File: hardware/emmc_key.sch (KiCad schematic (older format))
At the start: 7 parts, among them U1 EMMC Module

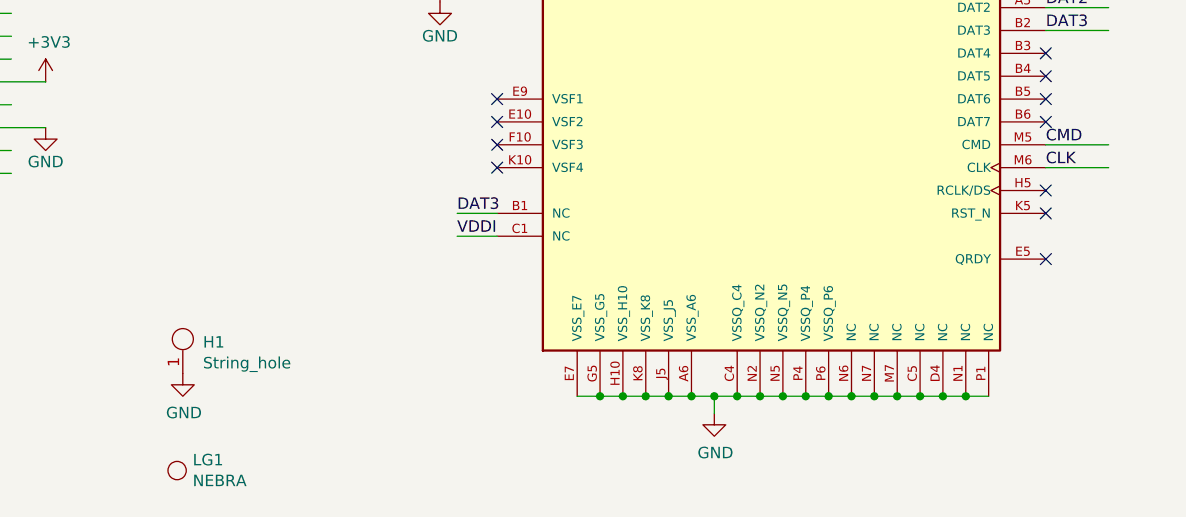
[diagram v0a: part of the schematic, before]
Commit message: RST_N connected to 3V3. Fabrication outputs regenerated.
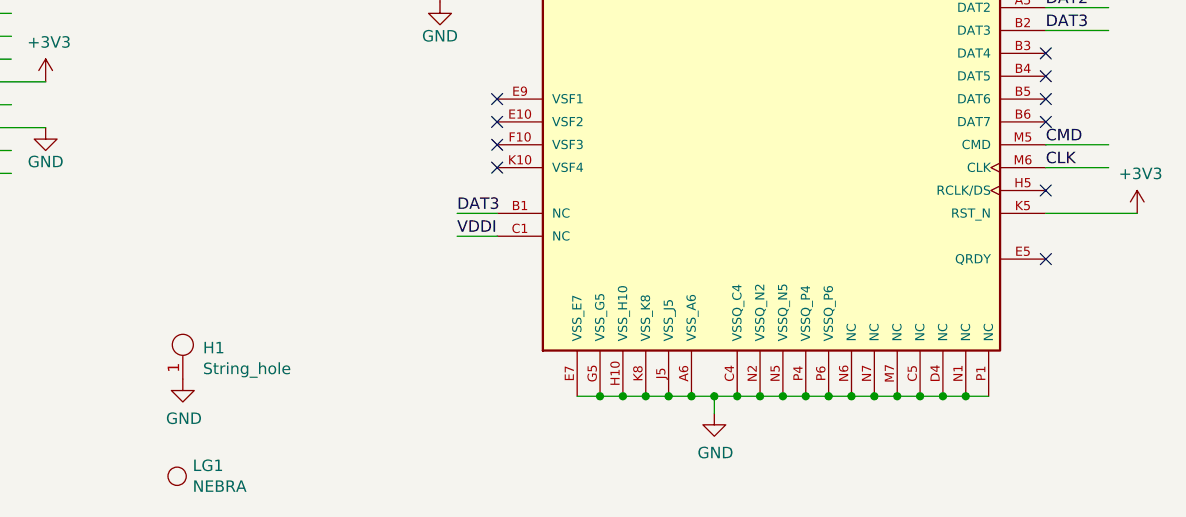
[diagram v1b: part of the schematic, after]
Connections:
- wire segments 54 -> 55
- no-connect marks 11 -> 10
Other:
- moved on the sheet: H1, LG1
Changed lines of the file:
@@
 NoConn ~ 7875 3750
 NoConn ~ 7875 4050
-NoConn ~ 7875 4150
 NoConn ~ 7875 4350
 NoConn ~ 5475 3850
@@
 L emms_key:String_hole H1
 U 1 1 607B301D
-P 4100 4700
-F 0 "H1" V 4114 4788 50  0000 L CNN
-F 1 "String_hole" V 4205 4788 50  0000 L CNN
-F 2 "MountingHole:MountingHole_2.2mm_M2" H 4100 4700 50  0001 C CNN
-F 3 "" H 4100 4700 50  0001 C CNN
-	1    4100 4700
+P 4100 4725
+F 0 "H1" V 4114 4813 50  0000 L CNN
+F 1 "String_hole" V 4205 4813 50  0000 L CNN
+F 2 "MountingHole:MountingHole_2.2mm_M2" H 4100 4725 50  0001 C CNN
+F 3 "" H 4100 4725 50  0001 C CNN
+	1    4100 4725
 	0    1    1    0
 $EndComp
@@
 L power:GND #PWR0108
 U 1 1 607B424A
-P 4100 4850
-F 0 "#PWR0108" H 4100 4600 50  0001 C CNN
-F 1 "GND" H 4105 4677 50  0000 C CNN
-F 2 "" H 4100 4850 50  0001 C CNN
-F 3 "" H 4100 4850 50  0001 C CNN
-	1    4100 4850
+P 4100 4875
+F 0 "#PWR0108" H 4100 4625 50  0001 C CNN
+F 1 "GND" H 4105 4702 50  0000 C CNN
+F 2 "" H 4100 4875 50  0001 C CNN
+F 3 "" H 4100 4875 50  0001 C CNN
+	1    4100 4875
 	1    0    0    -1
 $EndComp
@@
 L emms_key:Logo LG1
 U 1 1 607BEA9F
-P 4075 5275
-F 0 "LG1" H 4143 5321 50  0000 L CNN
-F 1 "NEBRA" H 4143 5230 50  0000 L CNN
-F 2 "emmc_key:NEBRA_LOGO" H 3895 5280 50  0001 C CNN
-F 3 "" H 3895 5280 50  0001 C CNN
-	1    4075 5275
+P 4075 5300
+F 0 "LG1" H 4143 5346 50  0000 L CNN
+F 1 "NEBRA" H 4143 5255 50  0000 L CNN
+F 2 "emmc_key:NEBRA_LOGO" H 3895 5305 50  0001 C CNN
+F 3 "" H 3895 5305 50  0001 C CNN
+	1    4075 5300
 	1    0    0    -1
 $EndComp
@@
 Wire Wire Line
 	7525 4950 7625 4950
+$Comp
+L power:+3V3 #PWR?
+U 1 1 60C0D36F
+P 8275 4150
+F 0 "#PWR?" H 8275 4000 50  0001 C CNN
+F 1 "+3V3" H 8290 4323 50  0000 C CNN
+F 2 "" H 8275 4150 50  0001 C CNN
+F 3 "" H 8275 4150 50  0001 C CNN
+	1    8275 4150
+	1    0    0    -1
+$EndComp
+Wire Wire Line
+	7875 4150 8275 4150
 $EndSCHEMATC

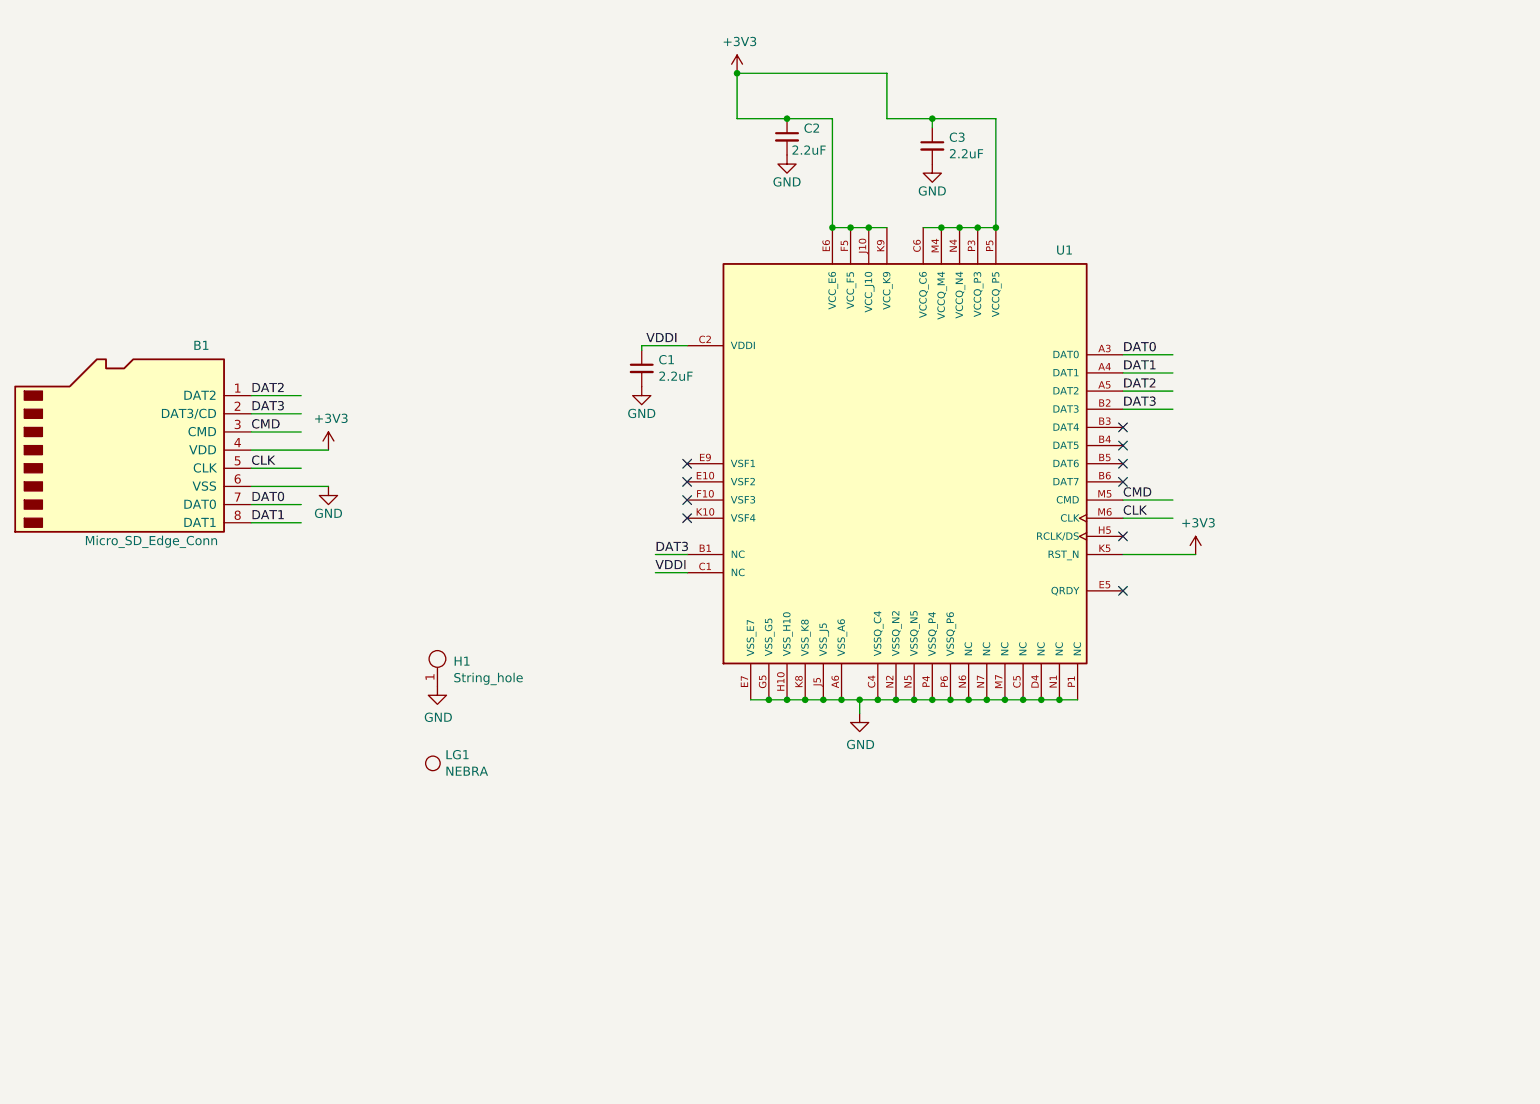
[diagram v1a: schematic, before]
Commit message: New variant with voltage translator and 1V8 LDO for eMMC modules where VCCQ is 1V8.
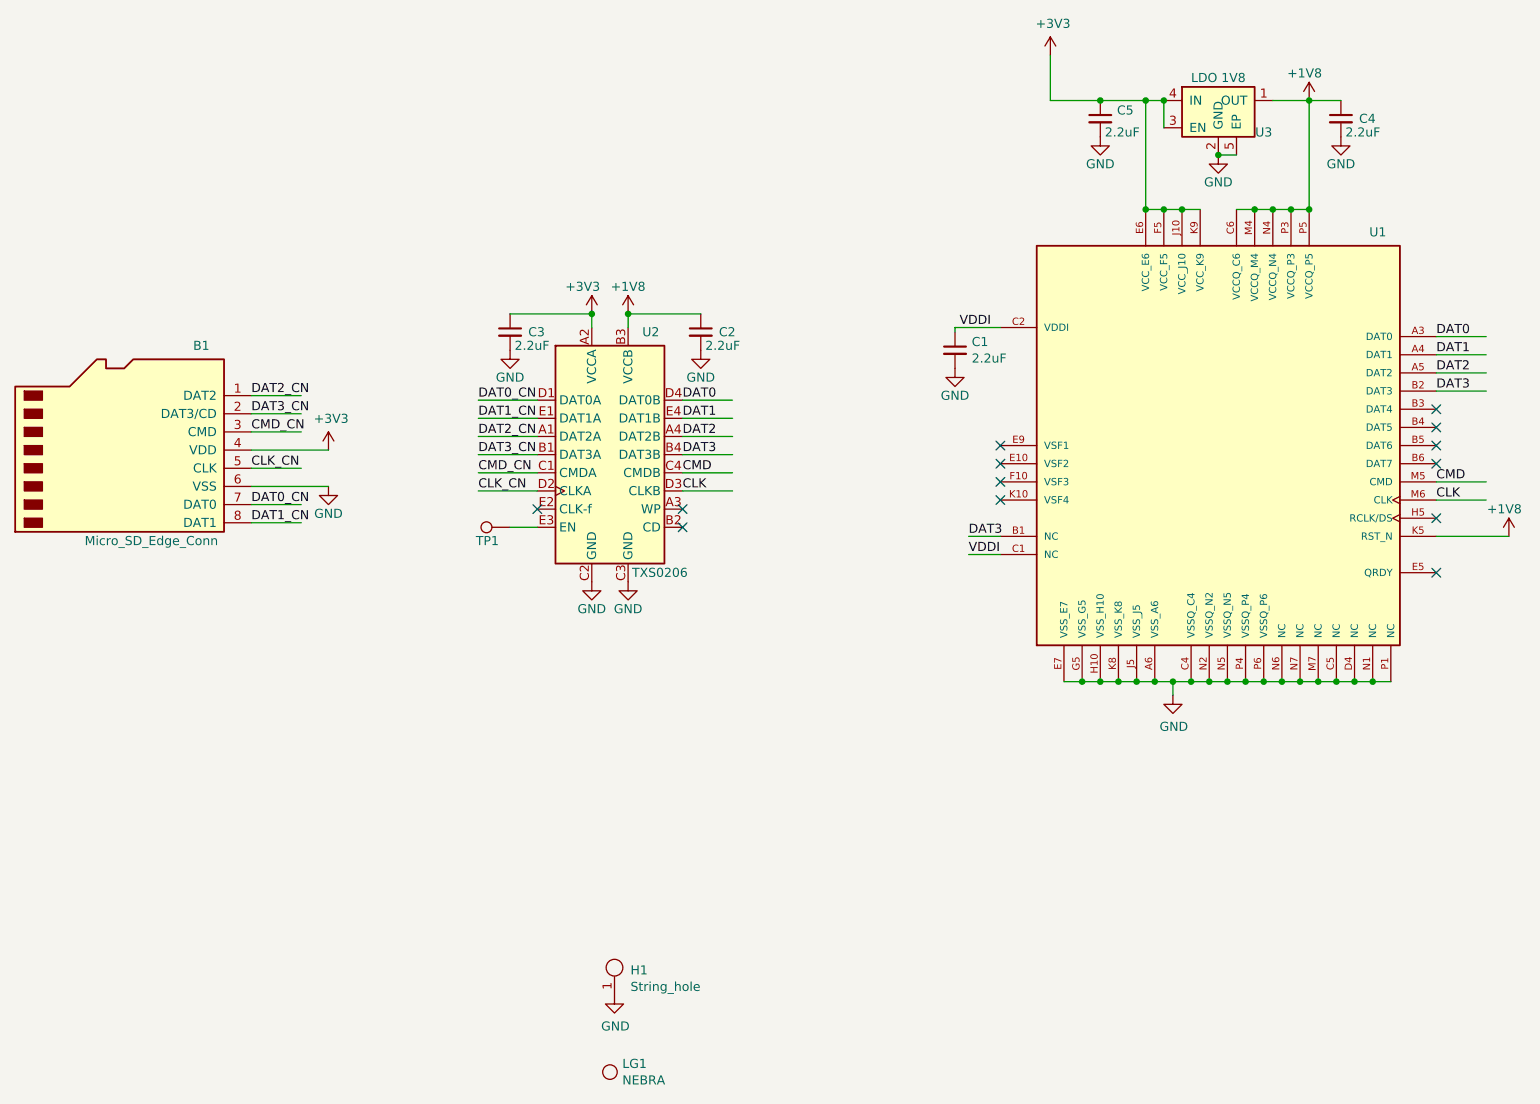
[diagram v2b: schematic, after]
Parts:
- added C2, C4: 2.2uF, Capacitor_SMD:C_0402_1005Metric, symbol Device:C_Small
- added TP1: TestPoint, TestPoint:TestPoint_Pad_D1.0mm, symbol Connector:TestPoint
- added U2: TXS0206, emmc_key:BGA20N40P5X4_195X155X50N, symbol emms_key:TXS0206
- added U3: LDO 1V8, Package_DFN_QFN:UDFN-4-1EP_1x1mm_P0.65mm_EP0.48x0.48mm, symbol emms_key:NCP177
- C1, C3: footprint Capacitor_SMD:C_0603_1608Metric -> Capacitor_SMD:C_0402_1005Metric; Manufacturer KEMET -> Samsung; Part Number C0603C225K8RACTU -> CL05A225MP5NSNC; Price [1k] 0.059 -> 0.045
- C5: renamed from C2; footprint Capacitor_SMD:C_0603_1608Metric -> Capacitor_SMD:C_0402_1005Metric; Manufacturer KEMET -> Samsung; Part Number C0603C225K8RACTU -> CL05A225MP5NSNC; Price [1k] 0.059 -> 0.045
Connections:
- net labels added: +1V8, CLK_CN, CMD_CN, DAT0_CN, DAT1_CN, DAT2_CN, DAT3_CN
- wire segments 55 -> 72
- no-connect marks 10 -> 13
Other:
- moved on the sheet: C1, C3, C5, H1, LG1, U1
